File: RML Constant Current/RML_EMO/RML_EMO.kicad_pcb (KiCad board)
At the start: 2 copper layers, 72 x 34 mm, 49 parts, among them J1 Tyco, J2 NANOFIT-4PIN, J3 Tyco, Q3 Q_NMOS_GSD, Q4 Q_NMOS_GSD, Q5 Q_NMOS_GSD, U1 LR8K4-G, U2 LM555xM, U5 LM1117DT-5.0, U6 Optocoupler, U7 74AHC1G02, U8 OPA1662DGK

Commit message: Current sink resistor change and DRC fix
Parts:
- moved R4 3.64 mm to (129.5, 87.5), turned to 90 degrees
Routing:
- net +5V: track 56.3 -> 69.3 mm
- net Net-(D2-K): track 22.7 -> 18.6 mm
- net CLOCK: track 16.8 -> 20.1 mm
- net GNDPWR: vias 15 -> 14
- net GND: vias 29 -> 28
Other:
- board text added: "RML"

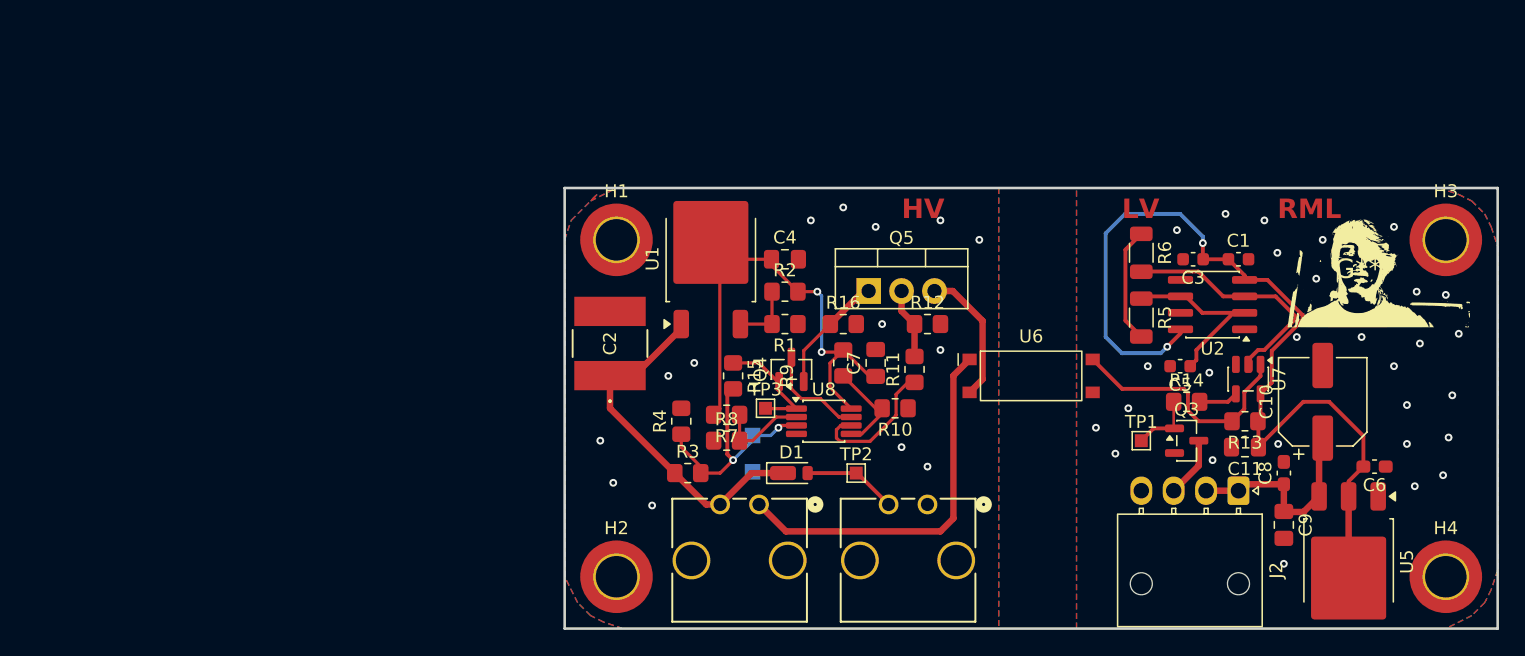
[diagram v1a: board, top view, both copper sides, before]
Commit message: added mouser# to HV side components
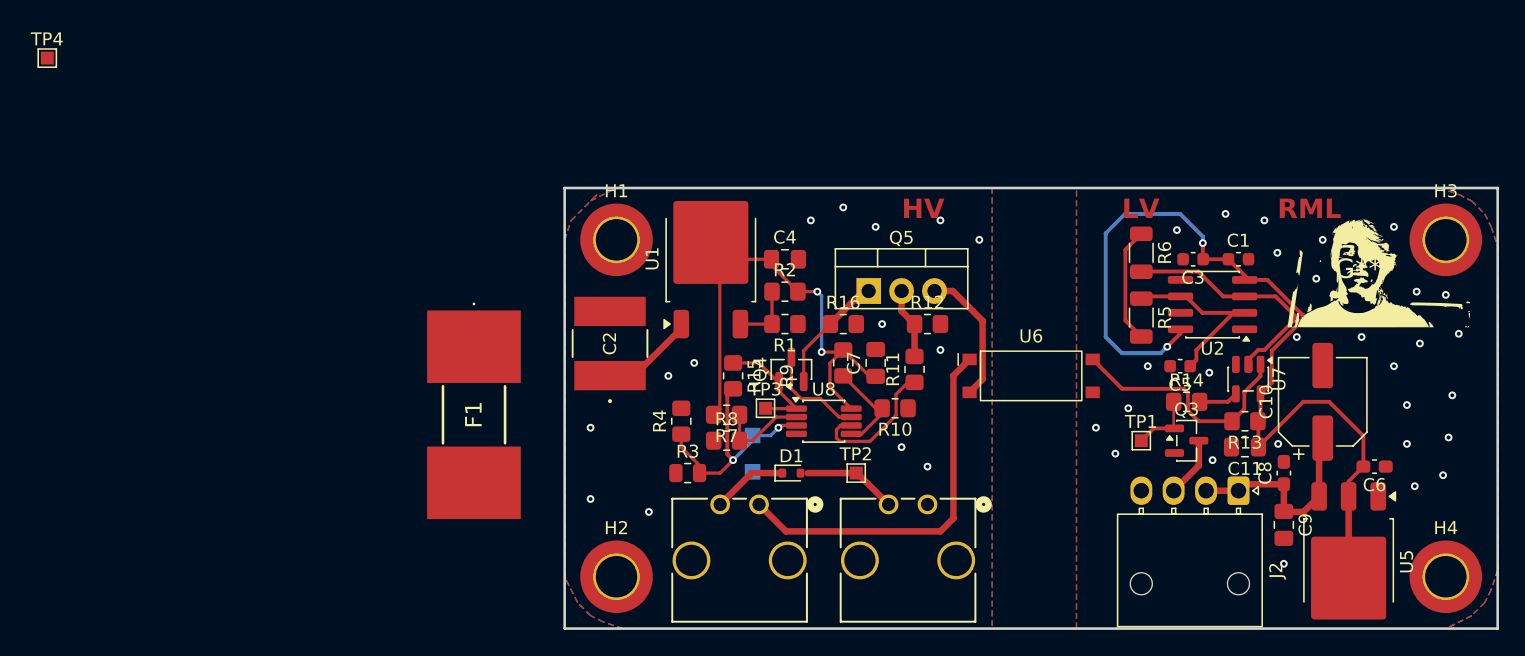
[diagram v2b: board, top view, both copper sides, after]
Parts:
- added F1: Fuse, Mouser:0885125DR, F.Cu at (113.5, 87.0)
- added TP4: TestPoint, TestPoint:TestPoint_Pad_1.0x1.0mm, F.Cu at (80.6, 59.5)
- D1: footprint Diode_SMD:D_TUMD2 -> Diode_SMD:D_SOD-523
- R11: value 100k -> 1M
- R12: value 1.8k -> 6k
- R3: value 400K -> 374k; footprint Resistor_SMD:R_0805_2012Metric_Pad1.20x1.40mm_HandSolder -> Resistor_SMD:R_0805_2012Metric
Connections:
- D1 pad 1: HVI+ -> Net-(D1-K)
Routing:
- net HVI+: track 27.3 -> 13.2 mm

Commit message: added bleeder resistor
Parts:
- removed F1: Fuse, Mouser:0885125DR
- removed TP4: TestPoint, TestPoint:TestPoint_Pad_1.0x1.0mm
- added R17: 1.5M, Resistor_SMD:R_2010_5025Metric_Pad1.40x2.65mm_HandSolder, F.Cu at (124.5, 83.5)
- R10: value 97.5k -> 86.6k
- R12: value 6k -> 6.04k
- R4: value 37K -> 36k
- R7: value 85.6k -> 86.6k
- R8: value 14.4k -> 14.3k
- R9: value 2.5k -> 2k
- moved C2 10.3 mm to (124.5, 91.8), turned to -90 degrees
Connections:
- net /5.17V renamed /5.10V
- D1 pad 1: Net-(D1-K) -> HVI+
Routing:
- net HVI+: track 13.2 -> 27.2 mm
- net GNDPWR: vias 14 -> 15

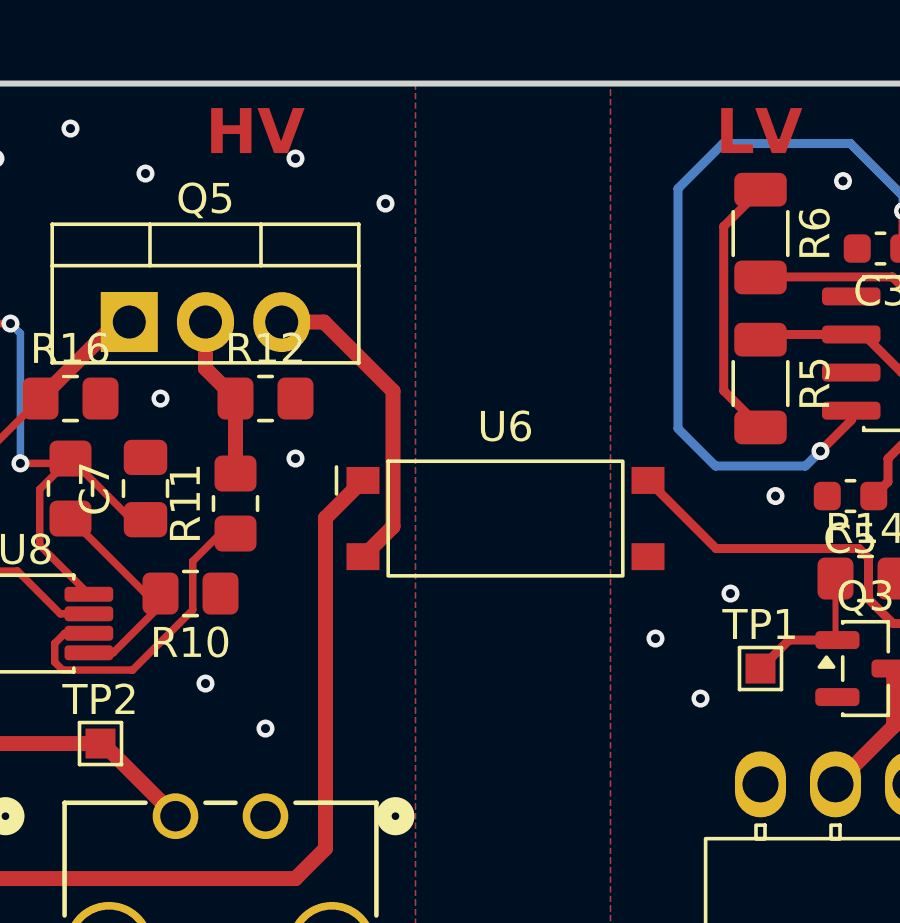
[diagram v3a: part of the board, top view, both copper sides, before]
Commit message: added manfacturer# to all components
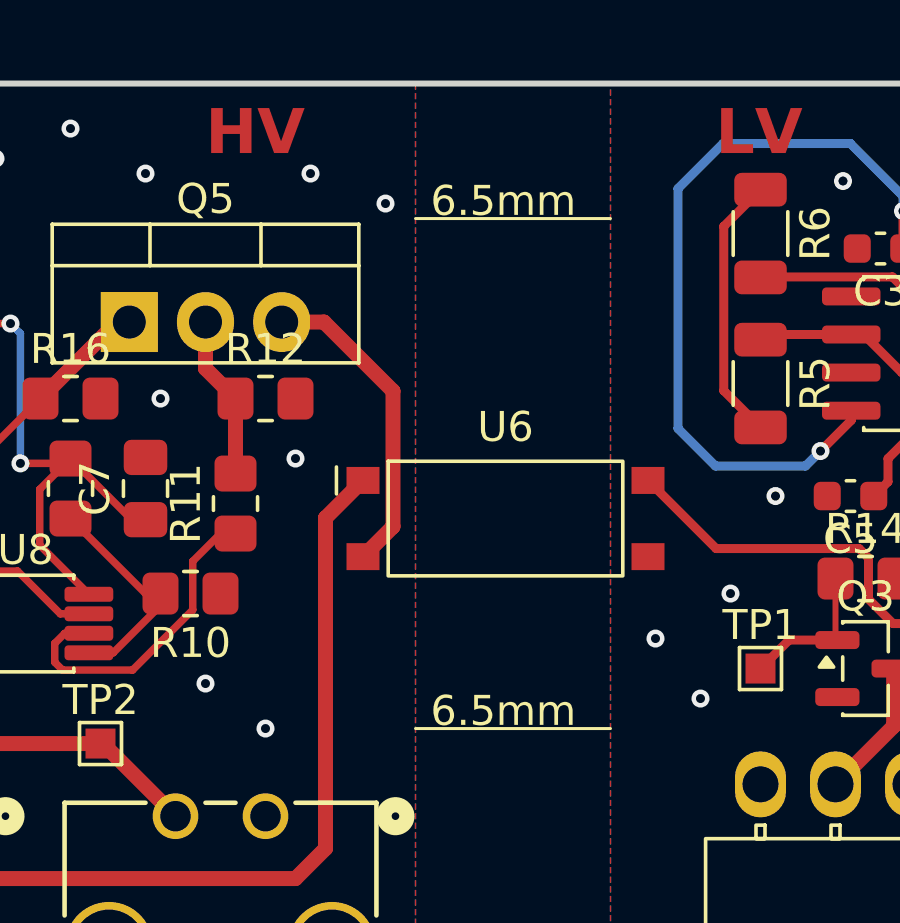
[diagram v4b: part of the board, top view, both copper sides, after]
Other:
- board text added: "6.5mm"
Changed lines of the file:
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@@
 		)
+	)
+	(gr_line
+		(start 153.5 74)
+		(end 160 74)
+		(stroke
+			(width 0.1)
+			(type default)
+		)
+		(layer "F.SilkS")
+	)
+	(gr_line
+		(start 153.5 91)
+		(end 160 91)
+		(stroke
+			(width 0.1)
+			(type default)
+		)
+		(layer "F.SilkS")
 	)
 	(gr_rect
@@
 		)
 	)
+	(gr_text "6.5mm"
+		(at 154 74 0)
+		(layer "F.SilkS")
+		(effects
+			(font
+				(size 1 1)
+				(thickness 0.1)
+			)
+			(justify left bottom)
+		)
+	)
+	(gr_text "6.5mm"
+		(at 154 91 0)
+		(layer "F.SilkS")
+		(effects
+			(font
+				(size 1 1)
+				(thickness 0.1)
+			)
+			(justify left bottom)
+		)
+	)
 	(segment
 		(start 124.506365 85.893635)
@@
 	)
 	(segment
-		(start 140.23514 85.75)
-		(end 141.66014 87.175)
-		(width 0.25)
-		(layer "F.Cu")
-		(net "Net-(Q4-D)")
-	)
-	(segment
-		(start 138.75 85.75)
-		(end 140.23514 85.75)
-		(width 0.25)
-		(layer "F.Cu")
-		(net "Net-(Q4-D)")
-	)
-	(segment
-		(start 138 85)
-		(end 138.75 85.75)
-		(width 0.25)
-		(layer "F.Cu")
-		(net "Net-(Q4-D)")
-	)
-	(segment
-		(start 138 82.5625)
-		(end 138 85)
-		(width 0.25)
-		(layer "F.Cu")
-		(net "Net-(Q4-D)")
-	)
-	(segment
-		(start 141.66014 87.175)
-		(end 142.6125 87.175)
-		(width 0.25)
-		(layer "F.Cu")
-		(net "Net-(Q4-D)")
-	)
-	(segment
 		(start 145.500001 93.921)
 		(end 143.079001 91.5)
@@
 		(layer "F.Cu")
 		(net "TS+")
+	)
+	(via
+		(at 145 80)
+		(size 0.6)
+		(drill 0.3)
+		(layers "F.Cu" "B.Cu")
+		(free yes)
+		(net "GNDPWR")
+	)
+	(via
+		(at 148.5 91)
+		(size 0.6)
+		(drill 0.3)
+		(layers "F.Cu" "B.Cu")
+		(free yes)
+		(net "GNDPWR")
+	)
+	(via
+		(at 126.5 86.5)
+		(size 0.6)
+		(drill 0.3)
+		(layers "F.Cu" "B.Cu")
+		(free yes)
+		(net "GNDPWR")
+	)
+	(via
+		(at 130.5 83)
+		(size 0.6)
+		(drill 0.3)
+		(layers "F.Cu" "B.Cu")
+		(free yes)
+		(net "GNDPWR")
+	)
+	(via
+		(at 142 71)
+		(size 0.6)
+		(drill 0.3)
+		(layers "F.Cu" "B.Cu")
+		(free yes)
+		(net "GNDPWR")
+	)
+	(via
+		(at 146.5 89.5)
+		(size 0.6)
+		(drill 0.3)
+		(layers "F.Cu" "B.Cu")
+		(free yes)
+		(net "GNDPWR")
+	)
+	(via
+		(at 122 86)
+		(size 0.6)
+		(drill 0.3)
+		(layers "F.Cu" "B.Cu")
+		(free yes)
+		(net "GNDPWR")
+	)
+	(via
+		(at 139.5 72)
+		(size 0.6)
+		(drill 0.3)
+		(layers "F.Cu" "B.Cu")
+		(free yes)
+		(net "GNDPWR")
+	)
+	(via
+		(at 152.5 73.5)
+		(size 0.6)
+		(drill 0.3)
+		(layers "F.Cu" "B.Cu")
+		(free yes)
+		(net "GNDPWR")
+	)
+	(via
+		(at 149.5 82)
+		(size 0.6)
+		(drill 0.3)
+		(layers "F.Cu" "B.Cu")
+		(free yes)
+		(net "GNDPWR")
+	)
+	(via
+		(at 150 72.5)
+		(size 0.6)
+		(drill 0.3)
+		(layers "F.Cu" "B.Cu")
+		(free yes)
+		(net "GNDPWR")
+	)
+	(via
+		(at 144.5 72.5)
+		(size 0.6)
+		(drill 0.3)
+		(layers "F.Cu" "B.Cu")
+		(free yes)
+		(net "GNDPWR")
+	)
+	(via
+		(at 127 96.5)
+		(size 0.6)
+		(drill 0.3)
+		(layers "F.Cu" "B.Cu")
+		(free yes)
+		(net "GNDPWR")
+	)
+	(via
+		(at 126.5 78.5)
+		(size 0.6)
+		(drill 0.3)
+		(layers "F.Cu" "B.Cu")
+		(free yes)
+		(net "GNDPWR")
+	)
+	(via
+		(at 123 79.5)
+		(size 0.6)
+		(drill 0.3)
+		(layers "F.Cu" "B.Cu")
+		(free yes)
+		(net "GNDPWR")
+	)
+	(segment
+		(start 134 87)
+		(end 134 89)
+		(width 0.25)
+		(layer "F.Cu")
+		(net "/5.10V")
+	)
+	(segment
+		(start 135 89)
+		(end 136.825 87.175)
+		(width 0.25)
+		(layer "F.Cu")
+		(net "/5.10V")
+	)
+	(segment
+		(start 134 89)
+		(end 135 89)
+		(width 0.25)
+		(layer "F.Cu")
+		(net "/5.10V")
+	)
+	(segment
+		(start 136.825 87.175)
+		(end 138.3875 87.175)
+		(width 0.25)
+		(layer "F.Cu")
+		(net "/5.10V")
 	)
 	(segment
@@
 		(net "/RML-")
 	)
-	(via
-		(at 145 80)
-		(size 0.6)
-		(drill 0.3)
-		(layers "F.Cu" "B.Cu")
-		(free yes)
-		(net "GNDPWR")
-	)
-	(via
-		(at 148.5 91)
-		(size 0.6)
-		(drill 0.3)
-		(layers "F.Cu" "B.Cu")
-		(free yes)
-		(net "GNDPWR")
-	)
-	(via
-		(at 126.5 86.5)
-		(size 0.6)
-		(drill 0.3)
-		(layers "F.Cu" "B.Cu")
-		(free yes)
-		(net "GNDPWR")
-	)
-	(via
-		(at 130.5 83)
-		(size 0.6)
-		(drill 0.3)
-		(layers "F.Cu" "B.Cu")
-		(free yes)
-		(net "GNDPWR")
-	)
-	(via
-		(at 142 71)
-		(size 0.6)
-		(drill 0.3)
-		(layers "F.Cu" "B.Cu")
-		(free yes)
-		(net "GNDPWR")
-	)
-	(via
-		(at 146.5 89.5)
-		(size 0.6)
-		(drill 0.3)
-		(layers "F.Cu" "B.Cu")
-		(free yes)
-		(net "GNDPWR")
-	)
-	(via
-		(at 122 86)
-		(size 0.6)
-		(drill 0.3)
-		(layers "F.Cu" "B.Cu")
-		(free yes)
-		(net "GNDPWR")
-	)
-	(via
-		(at 139.5 72)
-		(size 0.6)
-		(drill 0.3)
-		(layers "F.Cu" "B.Cu")
-		(free yes)
-		(net "GNDPWR")
-	)
-	(via
-		(at 152.5 73.5)
-		(size 0.6)
-		(drill 0.3)
-		(layers "F.Cu" "B.Cu")
-		(free yes)
-		(net "GNDPWR")
-	)
-	(via
-		(at 149.5 82)
-		(size 0.6)
-		(drill 0.3)
-		(layers "F.Cu" "B.Cu")
-		(free yes)
-		(net "GNDPWR")
-	)
-	(via
-		(at 149.5 72)
-		(size 0.6)
-		(drill 0.3)
-		(layers "F.Cu" "B.Cu")
-		(free yes)
-		(net "GNDPWR")
-	)
-	(via
-		(at 144.5 72.5)
-		(size 0.6)
-		(drill 0.3)
-		(layers "F.Cu" "B.Cu")
-		(free yes)
-		(net "GNDPWR")
-	)
-	(via
-		(at 127 96.5)
-		(size 0.6)
-		(drill 0.3)
-		(layers "F.Cu" "B.Cu")
-		(free yes)
-		(net "GNDPWR")
-	)
-	(via
-		(at 126.5 78.5)
-		(size 0.6)
-		(drill 0.3)
-		(layers "F.Cu" "B.Cu")
-		(free yes)
-		(net "GNDPWR")
-	)
-	(via
-		(at 123 79.5)
-		(size 0.6)
-		(drill 0.3)
-		(layers "F.Cu" "B.Cu")
-		(free yes)
-		(net "GNDPWR")
-	)
 	(segment
 		(start 175.068198 82.068198)
@@
 	)
 	(segment
+		(start 140.23514 85.75)
+		(end 141.66014 87.175)
+		(width 0.25)
+		(layer "F.Cu")
+		(net "Net-(Q4-D)")
+	)
+	(segment
+		(start 138.75 85.75)
+		(end 140.23514 85.75)
+		(width 0.25)
+		(layer "F.Cu")
+		(net "Net-(Q4-D)")
+	)
+	(segment
+		(start 138 85)
+		(end 138.75 85.75)
+		(width 0.25)
+		(layer "F.Cu")
+		(net "Net-(Q4-D)")
+	)
+	(segment
+		(start 138 82.5625)
+		(end 138 85)
+		(width 0.25)
+		(layer "F.Cu")
+		(net "Net-(Q4-D)")
+	)
+	(segment
+		(start 141.66014 87.175)
+		(end 142.6125 87.175)
+		(width 0.25)
+		(layer "F.Cu")
+		(net "Net-(Q4-D)")
+	)
+	(segment
 		(start 165.1725 77.865)
 		(end 165 78.0375)
@@
 		(net "Net-(R5-Pad2)")
 	)
-	(segment
-		(start 134 87)
-		(end 134 89)
-		(width 0.25)
-		(layer "F.Cu")
-		(net "/5.10V")
-	)
-	(segment
-		(start 135 89)
-		(end 136.825 87.175)
-		(width 0.25)
-		(layer "F.Cu")
-		(net "/5.10V")
-	)
-	(segment
-		(start 134 89)
-		(end 135 89)
-		(width 0.25)
-		(layer "F.Cu")
-		(net "/5.10V")
-	)
-	(segment
-		(start 136.825 87.175)
-		(end 138.3875 87.175)
-		(width 0.25)
-		(layer "F.Cu")
-		(net "/5.10V")
-	)
 	(zone

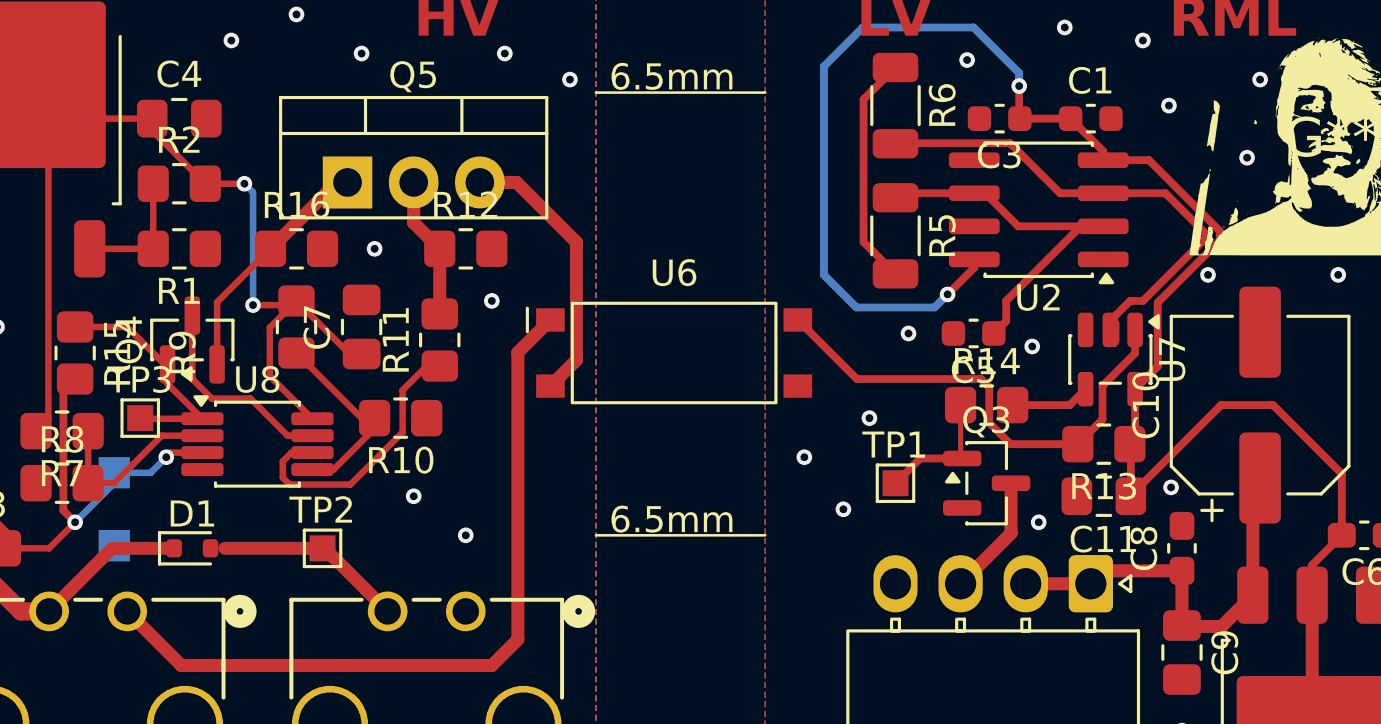
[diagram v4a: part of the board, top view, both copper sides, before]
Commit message: fixed decoupling cap issues
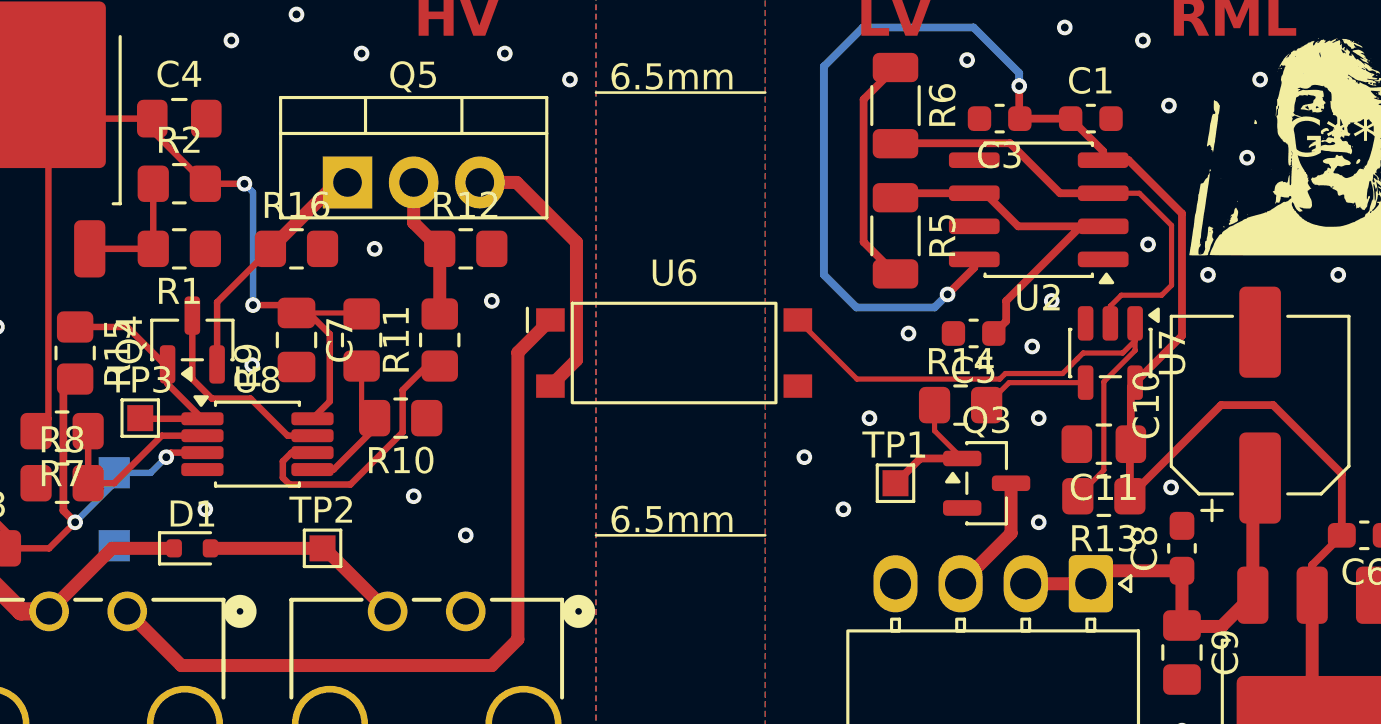
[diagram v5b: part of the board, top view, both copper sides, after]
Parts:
- moved C7 2.55 mm to (142.0, 83.5), turned to -90 degrees
- moved R9 2.55 mm to (144.5, 83.5)
- moved C11 2.00 mm to (173.0, 87.5)
- moved R13 2.00 mm to (173.0, 89.5)
- moved R14 1.00 mm to (167.5, 86.0)
- moved U7 0.25 mm to (173.2, 84.0)
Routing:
- net Net-(R13-Pad2): track 18.8 -> 22.7 mm
- net CLOCK: track 20.1 -> 18.1 mm
- net /35.1V: track 7.48 -> 5.65 mm
- net +5V: track 69.3 -> 67.6 mm
- net +36V: track 39.4 -> 38.1 mm
- net Net-(R14-Pad2): track 3.05 -> 4.16 mm
- net TS+: track 7.25 -> 7.80 mm
- net GNDPWR: vias 15 -> 17
- net GND: vias 28 -> 31
